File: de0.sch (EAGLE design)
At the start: 69 parts, among them IC1 PL2303SA__LF, J2 UX60SC-MB-5ST, U1 P0082, U2 RFM95W-915S2, U3 TPS76201DBVR, U4 TPS76201DBVR, U5 TPS76201DBVR

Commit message: Add files via upload
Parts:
- removed JP10: VDD, jumper:JP1Q
- removed JP8: VBP, jumper:JP1Q
- removed JP9: VBN, jumper:JP1Q
- added ADDRESS_0, ADDRESS_1, ADDRESS_10, ADDRESS_11, ADDRESS_12, ADDRESS_13, ADDRESS_14, ADDRESS_15, ADDRESS_2, ADDRESS_3, ADDRESS_4, ADDRESS_5, ADDRESS_6, ADDRESS_7, ADDRESS_8, ADDRESS_9, CLOCK, RD_DATA_0, RD_DATA_2, RD_DATA_3, RD_DATA_4, RD_DATA_5, RD_DATA_6, RD_DATA_7, RD_EN, U$4, U$40, U$48, U$49, U$50, U$51, U$52, U$53, USEC_TICK, WR_DATA_0, WR_DATA_1, WR_DATA_2, WR_DATA_3, WR_DATA_4, WR_DATA_5, WR_DATA_7, WR_EN: (no value), qfp160:POINT
- added C11, C13, C15, C20, C21, C22: 10uF, SparkFun-Capacitors:10UF-0603-6.3V-20%
- added C12, C14, C16, C17, C18, C19: 0.1uF, SparkFun-Capacitors:0.1UF-0603-25V-(+80/-20%)
- added J1: JUMPER_IN_50, jumper:J2X2MM
- added J3: REG_OUT_33, jumper:J2X2MM
- added JP13: REG_IN_07, jumper:JP1Q
- added JP14: REG_IN_12, jumper:JP1Q
- added JP15: REG_OUT_07, jumper:JP1Q
- added JP16: REG_OUT_12, jumper:JP1Q
- added JP17: VCCQ, jumper:JP1Q
- added JP18: VDDH, jumper:JP1Q
- added JP19: VDDLS, jumper:JP1Q
- added U$10: INTERRUPTS_0, qfp160:POINT
- added U$11: INTERRUPTS_1, qfp160:POINT
- added U$12: INTERRUPTS_2, qfp160:POINT
- added U$13: INTERRUPTS_3, qfp160:POINT
- added U$14, U$15: INTERRUPTS_5, qfp160:POINT
- added U$16: INTERRUPTS_6, qfp160:POINT
- added U$17: INTERRUPTS_7, qfp160:POINT
- JP3: value VDDLS -> VDD; device jumper:JP2Q -> jumper:JP1Q
- JP5: value LORA -> REG_IN_33; device jumper:JP6Q -> jumper:JP1Q
- JP6: value VCCQ -> VBP; device jumper:JP8Q -> jumper:JP1Q
- JP7: value VDDH -> VBN; device jumper:JP2Q -> jumper:JP1Q
- U$1: value (none) -> SOCKET
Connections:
- removed net N$12: JP2.7, U1G$2.GPIO_1_IN1
- removed net N$23: JP5.2, U2.MISO
- removed net N$25: JP5.6, U2.NSS
- removed net N$26: JP5.8, U2.RESET
- removed net N$28: JP5.12, U2.MOSI
- removed net N$37: JP5.10, U2.DIO0
- removed net VCCQ_0: JP6.2, U$1.P$49
- removed net VCCQ_1: JP6.4, U$1.P$62
- removed net VCCQ_2: JP6.6, U$1.P$83
- removed net VCCQ_3: JP6.8, U$1.P$93
- removed net VCCQ_4: JP6.10, U$1.P$105
- removed net VCCQ_5: JP6.12, U$1.P$114
- removed net VCCQ_6: JP6.14, U$1.P$135
- removed net VCCQ_7: JP6.16, U$1.P$145
- removed net VDDH_0: JP7.2, U$1.P$29
- removed net VDDH_1: JP7.4, U$1.P$99
- removed net VDDLS_0: JP3.2, U$1.P$33
- removed net VDDLS_1: JP3.4, U$1.P$103
- new net GPIO0_VCC_5V: J1.3, U1G$1.GPIO-0_VCC_SYS
- new net GPIO1_VCC_5V: U1G$2.GPIO-1_VCC_SYS
- new net IN_07: C9.1, JP13.2, U3.IN
- new net IN_12: C6.1, JP14.2, U4.IN
- new net IN_33: C3.1, JP5.2, U5.IN
- new net OUT_07: C10.1, JP15.1, R12.2, U3.OUT
- new net OUT_12: C7.1, JP16.1, R18.2, U4.OUT
- new net OUT_33: C4.1, J3.1, R19.2, U5.OUT
- new net VCCQ: C11.1, C12.1, JP17.2, U$1.P$105, U$1.P$114, U$1.P$135, U$1.P$145, U$1.P$49, U$1.P$62, U$1.P$83, U$1.P$93
- new net VDD5_USB: C2.+, D9.A, J1.1, J2.VCC
- new net VDDH: C13.1, C14.1, JP18.2, U$1.P$29, U$1.P$99
- new net VDDLS: C15.1, C16.1, JP19.2, U$1.P$103, U$1.P$33
- new net VO_FPGA_33: J3.3, U1G$1.GPIO-0_VCC3P3, U1G$2.GPIO-1_VCC3P3
- net ADDRESS_0: now also ADDRESS_0.P$1, U1G$1.GPIO_015; no longer U1G$1.GPIO_00
- net ADDRESS_1: now also ADDRESS_1.P$1, U1G$1.GPIO_017; no longer U1G$1.GPIO_01
- net ADDRESS_10: now also ADDRESS_10.P$1, U1G$1.GPIO_026; no longer U1G$1.GPIO_010
- net ADDRESS_11: now also ADDRESS_11.P$1, U1G$1.GPIO_028; no longer U1G$1.GPIO_011
- net ADDRESS_12: now also ADDRESS_12.P$1, U1G$1.GPIO_030; no longer U1G$1.GPIO_012
- net ADDRESS_13: now also ADDRESS_13.P$1, U1G$1.GPIO_032; no longer U1G$1.GPIO_013
- net ADDRESS_14: now also ADDRESS_14.P$1, U1G$1.GPIO_024; no longer U1G$1.GPIO_014
- net ADDRESS_15: now also ADDRESS_15.P$1, U1G$1.GPIO_022; no longer U1G$1.GPIO_016
- net ADDRESS_2: now also ADDRESS_2.P$1, U1G$1.GPIO_019; no longer U1G$1.GPIO_02
- net ADDRESS_3: now also ADDRESS_3.P$1, U1G$1.GPIO_021; no longer U1G$2.GPIO_124
- net ADDRESS_4: now also ADDRESS_4.P$1, U1G$1.GPIO_023; no longer U1G$1.GPIO_04
- net ADDRESS_5: now also ADDRESS_5.P$1, U1G$1.GPIO_025; no longer U1G$1.GPIO_05
- net ADDRESS_6: now also ADDRESS_6.P$1, U1G$1.GPIO_027; no longer U1G$1.GPIO_06
- net ADDRESS_7: now also ADDRESS_7.P$1, U1G$1.GPIO_029; no longer U1G$1.GPIO_07
- net ADDRESS_8: now also ADDRESS_8.P$1, U1G$1.GPIO_031; no longer U1G$1.GPIO_08
- net ADDRESS_9: now also ADDRESS_9.P$1, U1G$1.GPIO_033; no longer U1G$1.GPIO_09
- net CLOCK: now also CLOCK.P$1, U1G$2.GPIO_16; no longer U1G$2.GPIO_125
- net GND: now also C11.2, C12.2, C13.2, C14.2, C15.2, C16.2, C17.2, C18.2, C19.2, C20.2, C21.2, C22.2, JP7.1; no longer JP9.1
- net GPIO_OUT_0: now also U1G$2.GPIO_113; no longer U1G$1.GPIO_015
- net GPIO_OUT_1: now also U1G$2.GPIO_115; no longer U1G$2.GPIO_18
- net GPIO_OUT_2: now also U1G$2.GPIO_117; no longer U1G$2.GPIO_19
- net GPIO_OUT_3: now also U1G$2.GPIO_119; no longer U1G$2.GPIO_110
- net GPIO_OUT_4: now also U1G$2.GPIO_121; no longer U1G$2.GPIO_111
- net INTERRUPTS_0: now also U$10.P$1
- net INTERRUPTS_1: now also U$11.P$1
- net INTERRUPTS_2: now also U$12.P$1, U1G$2.GPIO_13; no longer U1G$2.GPIO_12
- net INTERRUPTS_3: now also U$13.P$1, U1G$2.GPIO_15; no longer U1G$2.GPIO_13
- net INTERRUPTS_4: now also U$14.P$1, U1G$2.GPIO_17; no longer U1G$2.GPIO_14
- net INTERRUPTS_5: now also U$15.P$1, U1G$2.GPIO_19; no longer U1G$2.GPIO_15
- net INTERRUPTS_6: now also U$16.P$1, U1G$2.GPIO_111; no longer U1G$2.GPIO_16
- net INTERRUPTS_7: now also U$17.P$1, U1G$1.GPIO_011; no longer U1G$2.GPIO_17
- net JTAG_TCK: now also U1G$1.GPIO_07; no longer U1G$2.GPIO_118
- net JTAG_TDI: now also U1G$1.GPIO_03; no longer U1G$2.GPIO_121
- net JTAG_TDO: now also U1G$1.GPIO_09; no longer U1G$2.GPIO_117
- net JTAG_TMS: now also U1G$1.GPIO_05; no longer U1G$2.GPIO_119
- net LORA_DIO0: now also U$53.P$1, U1G$2.GPIO_133, U2.DIO0; no longer JP5.9, U1G$2.GPIO_128
- net LORA_MISO: now also U$48.P$1, U1G$2.GPIO_123, U2.MISO; no longer JP5.1, U1G$2.GPIO_129
- net LORA_MOSI: now also U$49.P$1, U1G$2.GPIO_125, U2.MOSI; no longer JP5.11, U1G$2.GPIO_130
- net LORA_NSS: now also U$51.P$1, U1G$2.GPIO_129, U2.NSS; no longer JP5.5, U1G$2.GPIO_132
- net LORA_RESET: now also U$52.P$1, U1G$2.GPIO_131, U2.RESET; no longer JP5.7, U1G$2.GPIO_133
- net LORA_SCK: now also U$50.P$1, U1G$2.GPIO_127, U2.SCK; no longer JP5.3, U1G$2.GPIO_131
- net N$11: now also JP2.7; no longer JP2.5
- net N$24: now also JP2.5, U1G$2.GPIO_1_IN1; no longer JP5.4, U2.SCK
- net PIN_OUT_0: now also U1G$2.GPIO_120; no longer U1G$1.GPIO_03
- net PIN_OUT_2: now also U1G$2.GPIO_124; no longer U1G$2.GPIO_123
- net RD_DATA_0: now also RD_DATA_0.P$1, U1G$2.GPIO_118; no longer U1G$1.GPIO_025
- net RD_DATA_1: now also U$4.P$1, U1G$2.GPIO_116; no longer U1G$1.GPIO_026
- net RD_DATA_2: now also RD_DATA_2.P$1, U1G$2.GPIO_114; no longer U1G$1.GPIO_027
- net RD_DATA_3: now also RD_DATA_3.P$1, U1G$2.GPIO_112; no longer U1G$1.GPIO_028
- net RD_DATA_4: now also RD_DATA_4.P$1, U1G$2.GPIO_110; no longer U1G$1.GPIO_029
- net RD_DATA_5: now also RD_DATA_5.P$1, U1G$2.GPIO_18; no longer U1G$1.GPIO_030
- net RD_DATA_6: now also RD_DATA_6.P$1, U1G$2.GPIO_14; no longer U1G$1.GPIO_031
- net RD_DATA_7: now also RD_DATA_7.P$1, U1G$2.GPIO_12; no longer U1G$1.GPIO_032
- net RD_EN: now also RD_EN.P$1, U1G$1.GPIO_02; no longer U1G$2.GPIO_120
- net SPI_CS: now also U1G$2.GPIO_126; no longer U1G$2.GPIO_112
- net SPI_MISO: now also U1G$2.GPIO_128; no longer U1G$2.GPIO_114
- net SPI_MOSI: now also U1G$2.GPIO_130; no longer U1G$2.GPIO_115
- net SPI_SCK: now also U1G$2.GPIO_132; no longer U1G$2.GPIO_116
- net UART_RX: now also U1G$1.GPIO_01; no longer U1G$2.GPIO_126
- net UART_TX: now also U1G$1.GPIO_00; no longer U1G$2.GPIO_127
- net USEC_TICK: now also U1G$1.GPIO_013, USEC_TICK.P$1; no longer U1G$2.GPIO_113
- net VBN: now also C17.1, C21.1, JP7.2; no longer JP9.2
- net VBP: now also C18.1, C20.1, JP6.2; no longer JP8.2
- net VDD: now also C19.1, C22.1, JP3.2; no longer JP10.2
- net VDD5: now also J1.2, JP13.1, JP14.1, JP5.1; no longer C2.+, C3.1, C6.1, C9.1, D9.A, J2.VCC, U3.IN, U4.IN, U5.IN
- net VO_07: now also JP15.2, JP19.1; no longer C10.1, JP3.1, JP3.3, R12.2, U3.OUT
- net VO_12: now also JP16.2, JP18.1, JP3.1, JP6.1; no longer C7.1, JP10.1, JP7.1, JP7.3, JP8.1, R18.2, U4.OUT
- net VO_33: now also J3.2, JP17.1; no longer C4.1, JP6.1, JP6.11, JP6.13, JP6.15, JP6.3, JP6.5, JP6.7, JP6.9, R19.2, U5.OUT
- net WR_DATA_0: now also U1G$1.GPIO_018, WR_DATA_0.P$1; no longer U1G$1.GPIO_017
- net WR_DATA_1: now also U1G$1.GPIO_016, WR_DATA_1.P$1; no longer U1G$1.GPIO_018
- net WR_DATA_2: now also U1G$1.GPIO_014, WR_DATA_2.P$1; no longer U1G$1.GPIO_019
- net WR_DATA_3: now also U1G$1.GPIO_012, WR_DATA_3.P$1; no longer U1G$1.GPIO_020
- net WR_DATA_4: now also U1G$1.GPIO_010, WR_DATA_4.P$1; no longer U1G$1.GPIO_021
- net WR_DATA_5: now also U1G$1.GPIO_08, WR_DATA_5.P$1; no longer U1G$1.GPIO_022
- net WR_DATA_6: now also U$40.P$1, U1G$1.GPIO_06; no longer U1G$1.GPIO_023
- net WR_DATA_7: now also U1G$1.GPIO_04, WR_DATA_7.P$1; no longer U1G$1.GPIO_024
- net WR_EN: now also U1G$1.GPIO_020, WR_EN.P$1; no longer U1G$1.GPIO_033
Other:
- moved on the sheet: SV1, SV2, U2

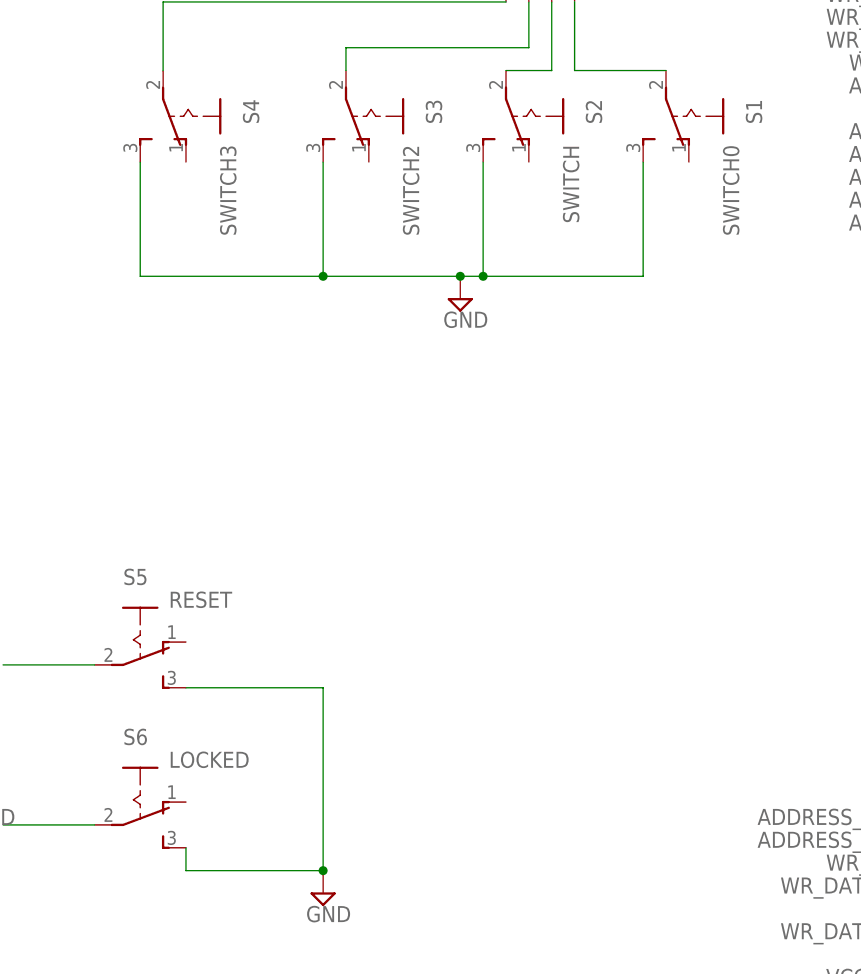
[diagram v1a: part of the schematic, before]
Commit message: Connect source for switches
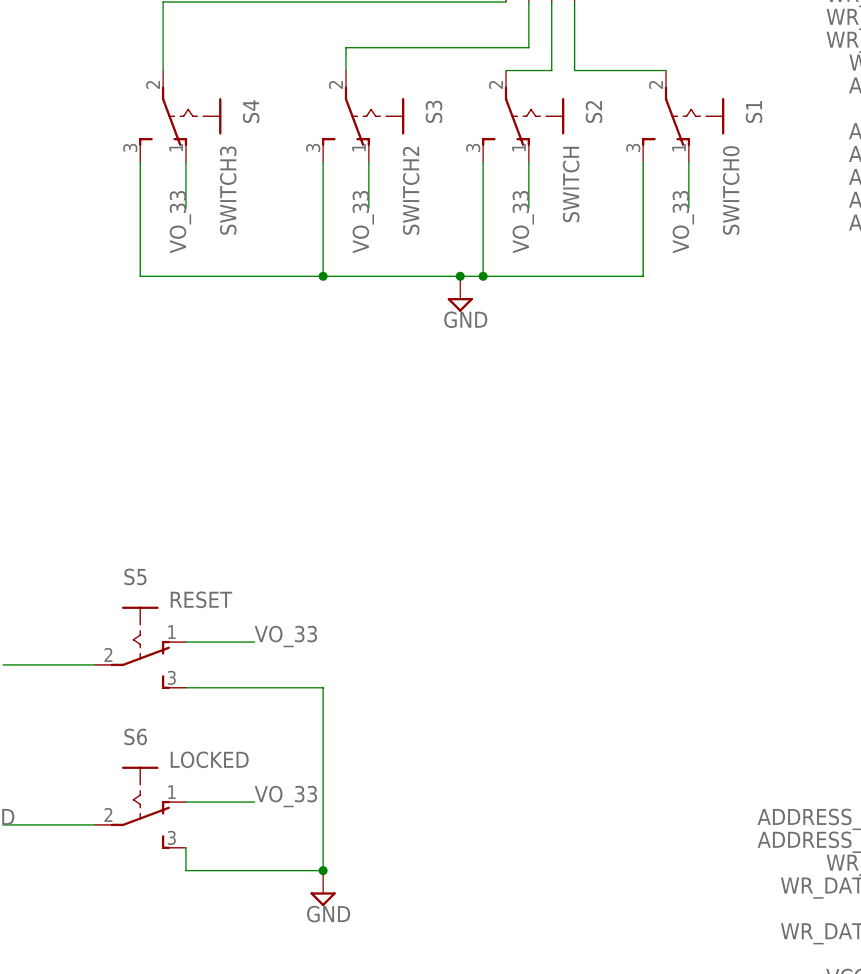
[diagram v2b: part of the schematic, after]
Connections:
- net VO_33: now also S1.O, S2.O, S3.O, S4.O, S5.O, S6.O
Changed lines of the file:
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@@
 <label x="292.1" y="-203.2" size="1.778" layer="95"/>
+</segment>
+<segment>
+<pinref part="S5" gate="1" pin="O"/>
+<wire x1="-76.2" y1="0" x2="-68.58" y2="0" width="0.1524" layer="91"/>
+<label x="-68.58" y="0" size="1.778" layer="95"/>
+</segment>
+<segment>
+<pinref part="S6" gate="1" pin="O"/>
+<wire x1="-76.2" y1="-17.78" x2="-68.58" y2="-17.78" width="0.1524" layer="91"/>
+<label x="-68.58" y="-17.78" size="1.778" layer="95"/>
+</segment>
+<segment>
+<pinref part="S4" gate="1" pin="O"/>
+<wire x1="-76.2" y1="53.34" x2="-76.2" y2="48.26" width="0.1524" layer="91"/>
+<label x="-76.2" y="43.18" size="1.778" layer="95" rot="R90"/>
+</segment>
+<segment>
+<pinref part="S3" gate="1" pin="O"/>
+<wire x1="-55.88" y1="53.34" x2="-55.88" y2="48.26" width="0.1524" layer="91"/>
+<label x="-55.88" y="43.18" size="1.778" layer="95" rot="R90"/>
+</segment>
+<segment>
+<pinref part="S2" gate="1" pin="O"/>
+<wire x1="-38.1" y1="53.34" x2="-38.1" y2="48.26" width="0.1524" layer="91"/>
+<label x="-38.1" y="43.18" size="1.778" layer="95" rot="R90"/>
+</segment>
+<segment>
+<pinref part="S1" gate="1" pin="O"/>
+<wire x1="-20.32" y1="53.34" x2="-20.32" y2="48.26" width="0.1524" layer="91"/>
+<label x="-20.32" y="43.18" size="1.778" layer="95" rot="R90"/>
 </segment>
 </net>

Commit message: Check USB and UART
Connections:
- net N$18 renamed D-
- net N$19 renamed D+
- new net N$20: C1.1, IC1.VO_33, R11.2
- new net VDD_USB: C2.+, D9.A, IC1.VDD_5, J2.VCC
- net VDD5: no longer IC1.VDD_5
- net VDD5_USB: no longer C2.+, D9.A, J2.VCC
- net VO_33: no longer C1.1, IC1.VO_33, R11.2
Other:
- note added: "LED USB Connector"
- note added: "USB Connector"
- note added: "USB TO UART"
- moved on the sheet: C1, C2, C5, C8, D9, IC1, J2, JP4, R10, R11, R22, R9

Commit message: Organize the schematic and the layout
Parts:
- removed C5, C8: 1nF, SparkFun-Capacitors:1.0NF/1000PF-0603-50V-10%
- removed J1: JUMPER_IN_50, jumper:J2X2MM
- removed J3: REG_OUT_33, jumper:J2X2MM
- removed JP1: JTAG PIN, pinhead:PINHD-2X10
- removed JP11: PIN_OUT, pinhead:PINHD-1X3
- removed JP13: REG_IN_07, jumper:JP1Q
- removed JP14: REG_IN_12, jumper:JP1Q
- removed JP15: REG_OUT_07, jumper:JP1Q
- removed JP16: REG_OUT_12, jumper:JP1Q
- removed JP17: VCCQ, jumper:JP1Q
- removed JP18: VDDH, jumper:JP1Q
- removed JP19: VDDLS, jumper:JP1Q
- removed JP2: SWITCH, jumper:JP4Q
- removed JP3: VDD, jumper:JP1Q
- removed JP4: UART, jumper:JP2Q
- removed JP5: REG_IN_33, jumper:JP1Q
- removed JP6: VBP, jumper:JP1Q
- removed JP7: VBN, jumper:JP1Q
- removed S5: RESET, switch:255SB
- removed S6: LOCKED, switch:255SB
- removed U$16: INTERRUPTS_6, qfp160:POINT
- added 5V_JUMPER: JUMPER_IN_50, jumper:J2X2MM
- added INTERRUPTS_6: INTERRUPTS_6, qfp160:POINT
- added JTAG: JTAG PIN, pinhead:PINHD-2X10
- added LOCKED: LOCKED, switch:255SB
- added PIN_OUT: PIN_OUT, pinhead:PINHD-1X3
- added REG_IN_07: REG_IN_07, jumper:JP1Q
- added REG_IN_12: REG_IN_12, jumper:JP1Q
- added REG_IN_33: REG_IN_33, jumper:JP1Q
- added REG_OUT_07: REG_OUT_07, jumper:JP1Q
- added REG_OUT_12: REG_OUT_12, jumper:JP1Q
- added REG_OUT_33: REG_OUT_33, jumper:J2X2MM
- added RESET: RESET, switch:255SB
- added SWITCH: SWITCH, jumper:JP4Q
- added UART_JUMPER: UART, jumper:JP2Q
- added VBN: VBN, jumper:JP1Q
- added VBP: VBP, jumper:JP1Q
- added VCCQ: VCCQ, jumper:JP1Q
- added VDD: VDD, jumper:JP1Q
- added VDDH: VDDH, jumper:JP1Q
- added VDDLS: VDDLS, jumper:JP1Q
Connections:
- removed net N$13: JP2.2, S1.P
- removed net N$14: JP2.4, S2.P
- removed net N$15: JP2.6, S3.P
- removed net N$16: JP2.8, S4.P
- removed net N$18: IC1.TXD, JP4.2
- removed net N$19: IC1.RXD, JP4.4
- removed net N$20 (its old number): C1.1, IC1.VO_33, R11.2
- removed net N$24: JP2.5, U1G$2.GPIO_1_IN1
- removed net VDD_USB: C2.+, D9.A, IC1.VDD_5, J2.VCC
- new net GPIO0_IN_0: SWITCH.1, U1G$1.GPIO_0_IN0
- new net GPIO0_IN_1: SWITCH.3, U1G$1.GPIO_0_IN1
- new net GPIO1_IN_0: SWITCH.7, U1G$2.GPIO_1_IN0
- new net GPIO1_IN_1: SWITCH.5, U1G$2.GPIO_1_IN1
- new net N$12: S1.P, SWITCH.2
- new net N$21: IC1.TXD, UART_JUMPER.2
- new net N$22: IC1.RXD, UART_JUMPER.4
- net GND: now also D1.C, D2.C, D3.C, D4.C, D5.C, D6.C, D7.C, D8.C, JTAG.10, JTAG.12, JTAG.14, JTAG.16, JTAG.18, JTAG.20, JTAG.4, JTAG.6, JTAG.8, LOCKED.S, RESET.S, U$1.P$35, U$1.P$67, VBN.1; no longer C5.1, C5.2, C8.1, C8.2, JP1.10, JP1.12, JP1.14, JP1.16, JP1.18, JP1.20, JP1.4, JP1.6, JP1.8, JP7.1, R1.1, R2.1, R3.1, R4.1, R5.1, R6.1, R7.1, R8.1, S5.S, S6.S
- net GPIO0_VCC_5V: now also 5V_JUMPER.3; no longer J1.3
- net GPIO_OUT_0: now also R1.2; no longer D1.A
- net GPIO_OUT_1: now also R2.2; no longer D2.A
- net GPIO_OUT_2: now also R3.2; no longer D3.A
- net GPIO_OUT_3: now also R4.2; no longer D4.A
- net GPIO_OUT_4: now also R5.2; no longer D5.A
- net INTERRUPTS_6: now also INTERRUPTS_6.P$1; no longer U$16.P$1
- net IN_07: now also REG_IN_07.2; no longer JP13.2
- net IN_12: now also REG_IN_12.2; no longer JP14.2
- net IN_33: now also REG_IN_33.2; no longer JP5.2
- net JTAG_TCK: now also JTAG.9; no longer JP1.9
- net JTAG_TDI: now also JTAG.5; no longer JP1.5
- net JTAG_TDO: now also JTAG.13; no longer JP1.13
- net JTAG_TMS: now also JTAG.7; no longer JP1.7
- net LOCKED: now also LOCKED.P; no longer S6.P
- net LORA_DIO0: now also R8.2; no longer D8.A
- net LORA_NSS: now also R6.2; no longer D6.A
- net LORA_RESET: now also R7.2; no longer D7.A
- net N$1: now also D1.A, R1.1; no longer D1.C, R1.2
- net N$10: now also S3.P, SWITCH.6; no longer JP2.3, U1G$1.GPIO_0_IN1
- net N$11: now also S2.P, SWITCH.4; no longer JP2.7, U1G$2.GPIO_1_IN0
- net N$2: now also D8.A, R8.1; no longer D2.C, R2.2
- net N$3: now also D7.A, R7.1; no longer D3.C, R3.2
- net N$4: now also D6.A, R6.1; no longer D4.C, R4.2
- net N$5: now also D5.A, R5.1; no longer D5.C, R5.2
- net N$6: now also D4.A, R4.1; no longer D6.C, R6.2
- net N$7: now also D2.A, R2.1; no longer D7.C, R7.2
- net N$8: now also D3.A, R3.1; no longer D8.C, R8.2
- net N$9: now also S4.P, SWITCH.8; no longer JP2.1, U1G$1.GPIO_0_IN0
- net OUT_07: now also REG_OUT_07.1; no longer JP15.1
- net OUT_12: now also REG_OUT_12.1; no longer JP16.1
- net OUT_33: now also REG_OUT_33.1; no longer J3.1
- net PIN_OUT_0: now also PIN_OUT.1; no longer JP11.1
- net PIN_OUT_1: now also PIN_OUT.2; no longer JP11.2
- net PIN_OUT_2: now also PIN_OUT.3; no longer JP11.3
- net RESET: now also RESET.P; no longer S5.P
- net UART_RX: now also UART_JUMPER.3; no longer JP4.3
- net UART_TX: now also UART_JUMPER.1; no longer JP4.1
- net VBN: now also VBN.2; no longer JP7.2
- net VBP: now also VBP.2; no longer JP6.2
- net VCCQ: now also VCCQ.2; no longer JP17.2
- net VDD: now also VDD.2; no longer JP3.2
- net VDD5: now also 5V_JUMPER.2, IC1.VDD_5, REG_IN_07.1, REG_IN_12.1, REG_IN_33.1; no longer J1.2, JP13.1, JP14.1, JP5.1
- net VDD5_USB: now also 5V_JUMPER.1, C2.+, D9.A, J2.VCC; no longer J1.1
- net VDDH: now also VDDH.2; no longer JP18.2
- net VDDLS: now also VDDLS.2; no longer JP19.2
- net VO_07: now also REG_OUT_07.2, VDDLS.1; no longer JP15.2, JP19.1
- net VO_12: now also REG_OUT_12.2, VBP.1, VDD.1, VDDH.1; no longer JP16.2, JP18.1, JP3.1, JP6.1
- net VO_33: now also C1.1, IC1.VO_33, LOCKED.O, R11.2, REG_OUT_33.2, RESET.O, VCCQ.1; no longer J3.2, JP17.1, S5.O, S6.O
- net VO_FPGA_33: now also REG_OUT_33.3; no longer J3.3
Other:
- note added: "8 x LED"
- note added: "CHIP SOURCE JUMPERS"
- note added: "FPGA CONNECTION"
- note added: "GND"
- note added: "JTAG"
- note added: "LoRa"
- note added: "PIN OUT"
- note added: "RESET & LOCKED SWITCH"
- note added: "Regulator - 5V to 0.7V"
- note added: "Regulator - 5V to 1.2V"
- note added: "Regulator - 5V to 3.3V"
- note added: "SOTB SOCKET"
- note added: "SPI"
- note added: "SWITCH IN"
- note added: "TEST POINTS"
- moved on the sheet: C1, C10, C11, C12, C13, C14, C15, C16, C17, C18, C19, C2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

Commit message: Update again schematic  for consistency
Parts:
- removed C2: 10uF, SparkFun-Capacitors:10UF-POLAR-0603-6.3V-20%(TANT)
- removed LOCKED: LOCKED, switch:255SB
- removed RESET: RESET, switch:255SB
- added C5: 10uF, SparkFun-Capacitors:10UF-0603-6.3V-20%
- added S5, S6: SS12SDP2, SamacSys_Parts:SS12SDP2
- S1: value SWITCH0 -> SS12SDP2; device switch:255SB -> SamacSys_Parts:SS12SDP2
- S2: value SWITCH -> SS12SDP2; device switch:255SB -> SamacSys_Parts:SS12SDP2
- S3: value SWITCH2 -> SS12SDP2; device switch:255SB -> SamacSys_Parts:SS12SDP2
- S4: value SWITCH3 -> SS12SDP2; device switch:255SB -> SamacSys_Parts:SS12SDP2
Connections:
- removed net N$10: S3.P, SWITCH.6
- removed net N$11: S2.P, SWITCH.4
- removed net N$12: S1.P, SWITCH.2
- removed net N$9: S4.P, SWITCH.8
- new net GPIO_0: S3.COM, SWITCH.2
- new net GPIO_1: S2.COM, SWITCH.4
- new net GPIO_2: S1.COM, SWITCH.6
- new net GPIO_3: S5.COM, SWITCH.8
- net GND: now also C5.2, S1.ON_2, S2.ON_2, S3.ON_2, S4.ON_2, S5.ON_2, S6.ON_2; no longer C2.-, LOCKED.S, RESET.S, S1.S, S2.S, S3.S, S4.S
- net LOCKED: now also S6.COM; no longer LOCKED.P
- net RESET: now also S4.COM; no longer RESET.P
- net VDD5_USB: now also C5.1; no longer C2.+
- net VO_33: now also S1.ON_1, S2.ON_1, S3.ON_1, S4.ON_1, S5.ON_1, S6.ON_1; no longer LOCKED.O, RESET.O, S1.O, S2.O, S3.O, S4.O

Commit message: change as Duran's suggest
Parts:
- removed U$48, U$49, U$50, U$51, U$52, U$53: (no value), qfp160:POINT
- added D10, D11, D12, D13, D14: LED0, SparkFun-LED:LED0603
- added JP1, JP2, JP3: (no value), jumper:JP1Q
- added Q1, Q2, Q3, Q4, Q5: AS9013-H-HF, SamacSys_Parts:AS9013-H-HF
- added R23, R24, R25, R26, R27: 330, SparkFun-Resistors:330OHM-0603-1/10W-1%
- added SV3, SV4: (no value), con-lstb:MA06-1
- REG_OUT_33: value REG_OUT_33 -> (none); device jumper:J2X2MM -> jumper:JP2Q
- renumbered S1 to SW2, S2 to SW1, S3 to SW0, S4 to RESET, S5 to SW3, S6 to LOCKED
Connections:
- new net LORA_ANT: SV4.6, U2.ANT
- new net LORA_DIO1: SV4.2, U2.DIO1
- new net LORA_DIO2: SV4.1, U2.DIO2
- new net LORA_DIO3: SV4.5, U2.DIO3
- new net LORA_DIO4: SV4.4, U2.DIO4
- new net LORA_DIO5: SV3.6, U2.DIO5
- new net N$10: D10.C, Q1.C
- new net N$11: D11.A, R24.1
- new net N$12: D11.C, Q2.C
- new net N$13: D12.A, R25.1
- new net N$14: D12.C, Q3.C
- new net N$15: D13.A, R26.1
- new net N$16: D13.C, Q4.C
- new net N$18: D14.A, R27.1
- new net N$19: D14.C, Q5.C
- new net N$23: JP1.2, R8.2
- new net N$24: JP2.2, R7.2
- new net N$25: JP3.2, R6.2
- new net N$9: D10.A, R23.1
- net GND: now also Q1.E, Q2.E, Q3.E, Q4.E, Q5.E
- net LORA_DIO0: now also JP1.1, SV4.3; no longer R8.2, U$53.P$1
- net LORA_MISO: now also SV3.1; no longer U$48.P$1
- net LORA_MOSI: now also SV3.2; no longer U$49.P$1
- net LORA_NSS: now also JP3.1, SV3.4; no longer R6.2, U$51.P$1
- net LORA_RESET: now also JP2.1, SV3.5; no longer R7.2, U$52.P$1
- net LORA_SCK: now also SV3.3; no longer U$50.P$1
- net OUT_33: now also REG_OUT_33.3; no longer REG_OUT_33.1
- net VCCQ: now also Q3.B
- net VO_07: now also Q4.B
- net VO_12: now also Q5.B
- net VO_33: now also Q1.B, REG_OUT_33.4
- net VO_FPGA_33: now also Q2.B, R23.2, R24.2, R25.2, R26.2, R27.2, REG_OUT_33.1; no longer REG_OUT_33.3
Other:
- moved on the sheet: U2
